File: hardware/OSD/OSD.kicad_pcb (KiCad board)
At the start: 2 copper layers, 16.9 x 21.7 mm, 36 parts, among them J1 Conn_01x06, J2 Conn_01x05, J3 S, J4 B, J5 B13, J6 W, J7 B1, J8 A5, Q1 MMBT3906, U1 SC662K-3.3V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

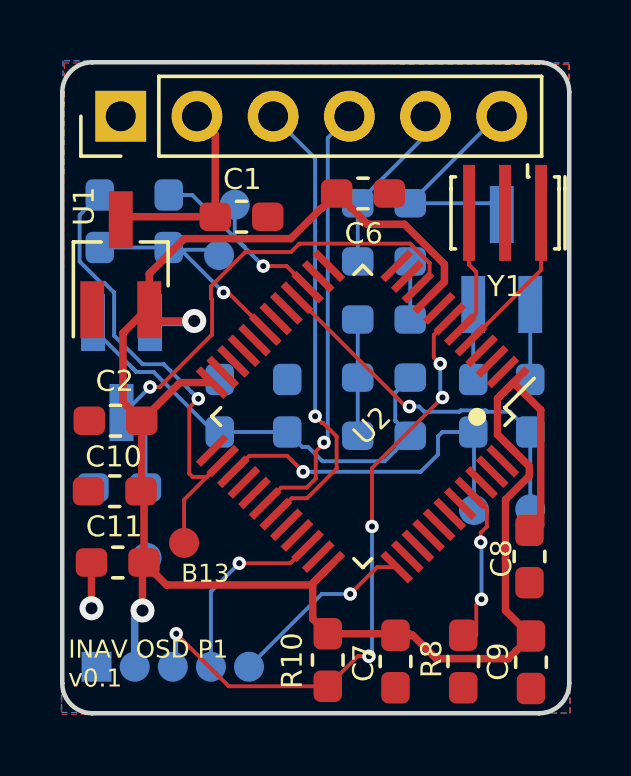
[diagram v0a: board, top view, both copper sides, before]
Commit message: Add a couple of leds
They could be useful for signaling status and/or errors
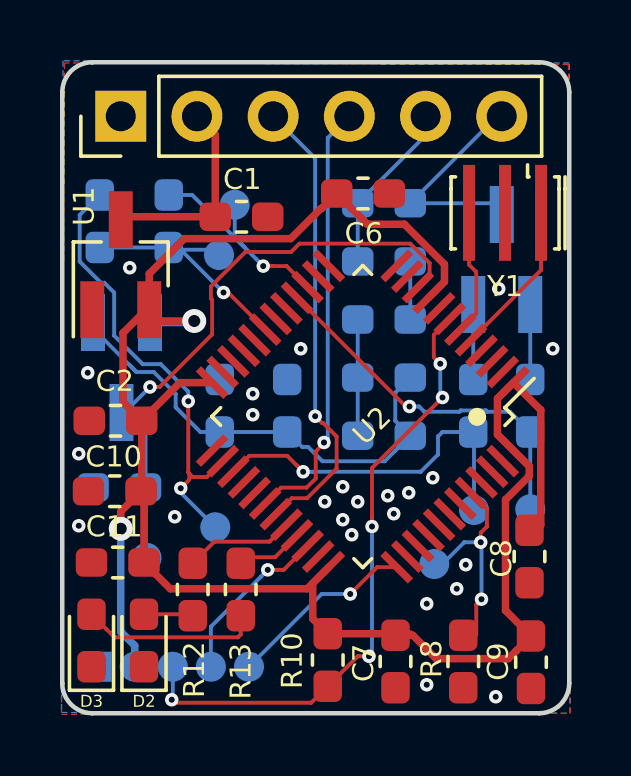
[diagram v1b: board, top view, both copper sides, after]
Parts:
- added D2: LED, LED_SMD:LED_0603_1608Metric_Pad1.05x0.95mm_HandSolder, F.Cu at (145.7, 71.7)
- added D3: LED, LED_SMD:LED_0603_1608Metric_Pad1.05x0.95mm_HandSolder, F.Cu at (143.9, 71.7)
- added J9: BOOT0, OSD:PinHeader_SMD_1x01_P1.27mm_Vertical, B.Cu at (155.3, 69.2)
- added R12: 100, Resistor_SMD:R_0603_1608Metric_Pad1.05x0.95mm_HandSolder, F.Cu at (147.3, 70.0)
- added R13: 100, Resistor_SMD:R_0603_1608Metric_Pad1.05x0.95mm_HandSolder, F.Cu at (148.9, 70.0)
- J5: moved to B.Cu
- moved J5 1.16 mm to (148.1, 68.0)
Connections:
- net Net-(R8-Pad1) renamed /BOOT0
- U2 pad 32: Net-(U2-Pad32) -> /LED1
- U2 pad 33: Net-(U2-Pad33) -> /LED2
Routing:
- net Net-(D3-Pad2): track 0.00 -> 5.96 mm
- net /LED1: track 0.00 -> 3.65 mm
- net +3V3: track 64.9 -> 67.7 mm
- net /LED2: track 0.00 -> 2.55 mm
- net Net-(D2-Pad2): track 0.00 -> 1.65 mm
- net GND: track 1.53 -> 0.00 mm, vias 1 -> 24
- net /BOOT0: track 5.13 -> 6.53 mm
- net /PB13: track 16.6 -> 15.5 mm, vias 1 -> 2
- net /SWDIO: track 6.36 -> 5.67 mm
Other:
- board text added: "INAVOSD P1 v0.1"
- board text removed: "INAV OSD P1 v0.1"
- board text removed: "inavflight.com"

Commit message: Change BLACK and WHITE resistors to 330
4k7 makes the OSD too faint
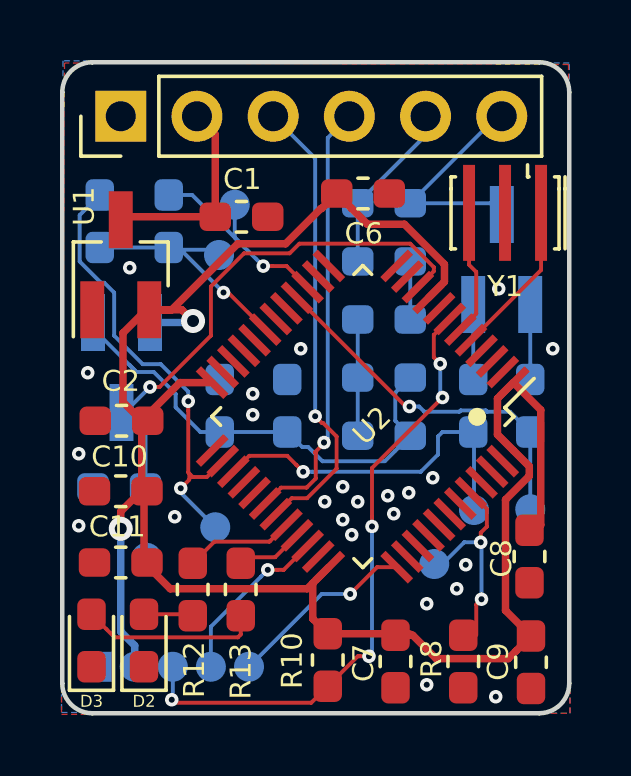
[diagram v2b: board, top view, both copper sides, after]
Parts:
- R5, R6: value 4k7 -> 330
- moved C10 0.20 mm to (144.9, 66.8)
- moved C2 0.20 mm to (144.9, 64.4)
- moved C11 0.10 mm to (144.9, 69.1)
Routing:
- net +3V3: track 67.7 -> 66.9 mm
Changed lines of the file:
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@@
     (thickness 1.6)
     (drawings 21)
-    (tracks 293)
+    (tracks 291)
     (zones 0)
     (modules 41)
@@
   )
   (module Capacitor_SMD:C_0603_1608Metric_Pad1.05x0.95mm_HandSolder (layer F.Cu)
-    (at 144.7 66.75 180)
+    (at 144.9 66.75 180)
     (descr "Capacitor SMD 0603 (1608 Metric), square (rectangular) end terminal, IPC_7351 nominal with elongated pad for handsoldering. (Body size source: http://www.tortai-tech.com/upload/download/2011102023233369053.pdf), generated with kicad-footprint-generator")
     (tags "capacitor handsolder")
@@
   )
   (module Capacitor_SMD:C_0603_1608Metric_Pad1.05x0.95mm_HandSolder (layer F.Cu)
-    (at 144.725 64.4 180)
+    (at 144.925 64.4 180)
     (descr "Capacitor SMD 0603 (1608 Metric), square (rectangular) end terminal, IPC_7351 nominal with elongated pad for handsoldering. (Body size source: http://www.tortai-tech.com/upload/download/2011102023233369053.pdf), generated with kicad-footprint-generator")
     (tags "capacitor handsolder")
@@
   )
   (module Capacitor_SMD:C_0603_1608Metric_Pad1.05x0.95mm_HandSolder (layer F.Cu)
-    (at 144.8 69.125 180)
+    (at 144.9 69.125 180)
     (descr "Capacitor SMD 0603 (1608 Metric), square (rectangular) end terminal, IPC_7351 nominal with elongated pad for handsoldering. (Body size source: http://www.tortai-tech.com/upload/download/2011102023233369053.pdf), generated with kicad-footprint-generator")
     (tags "capacitor handsolder")
@@
       (effects (font (size 0.7 0.7) (thickness 0.12)) (justify mirror))
     )
-    (fp_text value 4k7 (at 0 -1.43 90) (layer B.Fab)
+    (fp_text value 330 (at 0 -1.43 90) (layer B.Fab)
       (effects (font (size 0.7 0.7) (thickness 0.12)) (justify mirror))
     )
@@
       (effects (font (size 0.7 0.7) (thickness 0.12)) (justify mirror))
     )
-    (fp_text value 4k7 (at 0 -1.43 90) (layer B.Fab)
+    (fp_text value 330 (at 0 -1.43 90) (layer B.Fab)
       (effects (font (size 0.7 0.7) (thickness 0.12)) (justify mirror))
     )
@@
   (segment (start 148.05 54.86) (end 147.44 54.25) (width 0.25) (layer F.Cu) (net 2) (status 30))
   (segment (start 148.05 57.6) (end 148.05 54.86) (width 0.25) (layer F.Cu) (net 2) (status 30))
-  (via (at 147.35 61.075) (size 0.8) (drill 0.4) (layers F.Cu B.Cu) (net 3))
-  (segment (start 147.3 61.125) (end 147.35 61.075) (width 0.25) (layer B.Cu) (net 3))
-  (segment (start 145.875 61.125) (end 147.3 61.125) (width 0.25) (layer B.Cu) (net 3) (status 10))
-  (segment (start 146.225 61.075) (end 145.85 60.7) (width 0.25) (layer F.Cu) (net 3) (status 30))
-  (segment (start 147.35 61.075) (end 146.225 61.075) (width 0.25) (layer F.Cu) (net 3) (status 20))
   (segment (start 145.6 66.675) (end 145.7 66.775) (width 0.25) (layer F.Cu) (net 3))
   (segment (start 145.6 64.4) (end 145.6 66.675) (width 0.25) (layer F.Cu) (net 3))
@@
   (segment (start 152.599072 57.324072) (end 152.1 56.825) (width 0.25) (layer F.Cu) (net 3))
   (segment (start 155.158936 60.300126) (end 155.689265 59.769797) (width 0.25) (layer F.Cu) (net 3))
-  (segment (start 151.573366 57.324072) (end 151.600928 57.324072) (width 0.25) (layer F.Cu) (net 3))
-  (segment (start 150.567428 58.33001) (end 151.573366 57.324072) (width 0.25) (layer F.Cu) (net 3))
-  (segment (start 147.01999 58.33001) (end 150.567428 58.33001) (width 0.25) (layer F.Cu) (net 3))
-  (segment (start 145.85 59.5) (end 147.01999 58.33001) (width 0.25) (layer F.Cu) (net 3))
-  (segment (start 151.600928 57.324072) (end 152.1 56.825) (width 0.25) (layer F.Cu) (net 3))
-  (segment (start 145.85 60.7) (end 145.85 59.5) (width 0.25) (layer F.Cu) (net 3))
   (segment (start 157.725 70.725) (end 158.575 71.575) (width 0.25) (layer F.Cu) (net 3))
   (segment (start 157.725 67.032532) (end 157.725 70.725) (width 0.25) (layer F.Cu) (net 3))
@@
   (segment (start 146.55 70) (end 151.115916 70) (width 0.25) (layer F.Cu) (net 3))
   (segment (start 145.675 69.125) (end 146.55 70) (width 0.25) (layer F.Cu) (net 3))
+  (segment (start 151.600928 57.324072) (end 152.1 56.825) (width 0.25) (layer F.Cu) (net 3))
+  (segment (start 150.397438 58.5) (end 151.573366 57.324072) (width 0.25) (layer F.Cu) (net 3))
+  (segment (start 148.8 58.5) (end 150.397438 58.5) (width 0.25) (layer F.Cu) (net 3))
+  (segment (start 145.85 60.7) (end 146.6 60.7) (width 0.25) (layer F.Cu) (net 3))
+  (segment (start 146.6 60.7) (end 148.8 58.5) (width 0.25) (layer F.Cu) (net 3))
+  (segment (start 151.573366 57.324072) (end 151.600928 57.324072) (width 0.25) (layer F.Cu) (net 3))
+  (segment (start 145.875 61.125) (end 147.259989 61.125) (width 0.25) (layer B.Cu) (net 3))
+  (segment (start 147.259989 61.125) (end 147.309989 61.075) (width 0.25) (layer B.Cu) (net 3))
+  (via (at 147.309989 61.075) (size 0.8) (drill 0.4) (layers F.Cu B.Cu) (net 3))
+  (segment (start 145.85 60.7) (end 146.934989 60.7) (width 0.25) (layer F.Cu) (net 3))
+  (segment (start 146.934989 60.7) (end 147.309989 61.075) (width 0.25) (layer F.Cu) (net 3))
   (segment (start 152.8 61.025) (end 152.8 62.9625) (width 0.13) (layer B.Cu) (net 4) (status 30))
   (segment (start 152.8 62.9625) (end 152.8 64.9) (width 0.13) (layer B.Cu) (net 4) (status 30))
@@
   (segment (start 145.025 64.125) (end 144.925 64.125) (width 0.13) (layer B.Cu) (net 16))
   (segment (start 145.875 63.275) (end 145.025 64.125) (width 0.13) (layer B.Cu) (net 16))
-  (segment (start 146.193198 63.275) (end 145.875 63.275) (width 0.13) (layer F.Cu) (net 16))
-  (segment (start 147.904999 60.326601) (end 147.945001 60.366603) (width 0.13) (layer F.Cu) (net 16))
-  (segment (start 147.945001 61.523197) (end 146.193198 63.275) (width 0.13) (layer F.Cu) (net 16))
-  (segment (start 147.904999 59.923399) (end 147.904999 60.326601) (width 0.13) (layer F.Cu) (net 16))
-  (segment (start 147.945001 60.366603) (end 147.945001 61.523197) (width 0.13) (layer F.Cu) (net 16))
-  (segment (start 149.053398 58.775) (end 147.904999 59.923399) (width 0.13) (layer F.Cu) (net 16))
-  (segment (start 150.575 58.775) (end 149.053398 58.775) (width 0.13) (layer F.Cu) (net 16))
-  (segment (start 150.853552 58.496448) (end 150.575 58.775) (width 0.13) (layer F.Cu) (net 16))
-  (segment (start 154.550284 58.496448) (end 150.853552 58.496448) (width 0.13) (layer F.Cu) (net 16))
-  (segment (start 155.194847 59.141011) (end 154.550284 58.496448) (width 0.13) (layer F.Cu) (net 16))
-  (segment (start 155.194847 59.557109) (end 155.194847 59.141011) (width 0.13) (layer F.Cu) (net 16))
-  (segment (start 154.805383 59.946573) (end 155.194847 59.557109) (width 0.13) (layer F.Cu) (net 16))
   (segment (start 145.725 68.935) (end 145.76 68.97) (width 0.13) (layer B.Cu) (net 16))
   (segment (start 145.725 66.625) (end 145.725 68.935) (width 0.13) (layer B.Cu) (net 16))
+  (segment (start 147.904999 61.563199) (end 146.193198 63.275) (width 0.13) (layer F.Cu) (net 16))
+  (segment (start 147.904999 59.923399) (end 147.904999 61.563199) (width 0.13) (layer F.Cu) (net 16))
+  (segment (start 149.008387 58.820011) (end 147.904999 59.923399) (width 0.13) (layer F.Cu) (net 16))
+  (segment (start 150.52999 58.820011) (end 149.008387 58.820011) (width 0.13) (layer F.Cu) (net 16))
+  (segment (start 150.853552 58.496448) (end 150.52999 58.820011) (width 0.13) (layer F.Cu) (net 16))
+  (segment (start 154.550284 58.496448) (end 150.853552 58.496448) (width 0.13) (layer F.Cu) (net 16))
+  (segment (start 146.193198 63.275) (end 145.875 63.275) (width 0.13) (layer F.Cu) (net 16))
+  (segment (start 155.335712 59.281876) (end 154.550284 58.496448) (width 0.13) (layer F.Cu) (net 16))
+  (segment (start 155.335712 59.416244) (end 155.335712 59.281876) (width 0.13) (layer F.Cu) (net 16))
+  (segment (start 154.805383 59.946573) (end 155.335712 59.416244) (width 0.13) (layer F.Cu) (net 16))
   (via (at 154.525 63.925) (size 0.45) (drill 0.2) (layers F.Cu B.Cu) (net 17))
   (segment (start 150.774874 60.300126) (end 154.399748 63.925) (width 0.13) (layer F.Cu) (net 17))
